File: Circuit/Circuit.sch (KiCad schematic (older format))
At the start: 47 parts, among them J1 Conn_01x20, J2 Conn_01x20, Q1 Q_NMOS_GDS, U1 STM32F103C8Tx, U2 AP131-33, U3 MCP2551-I-P, U4 MCP23017, U5 MC34063AP, Y1 8.000M, Y2 32.768K

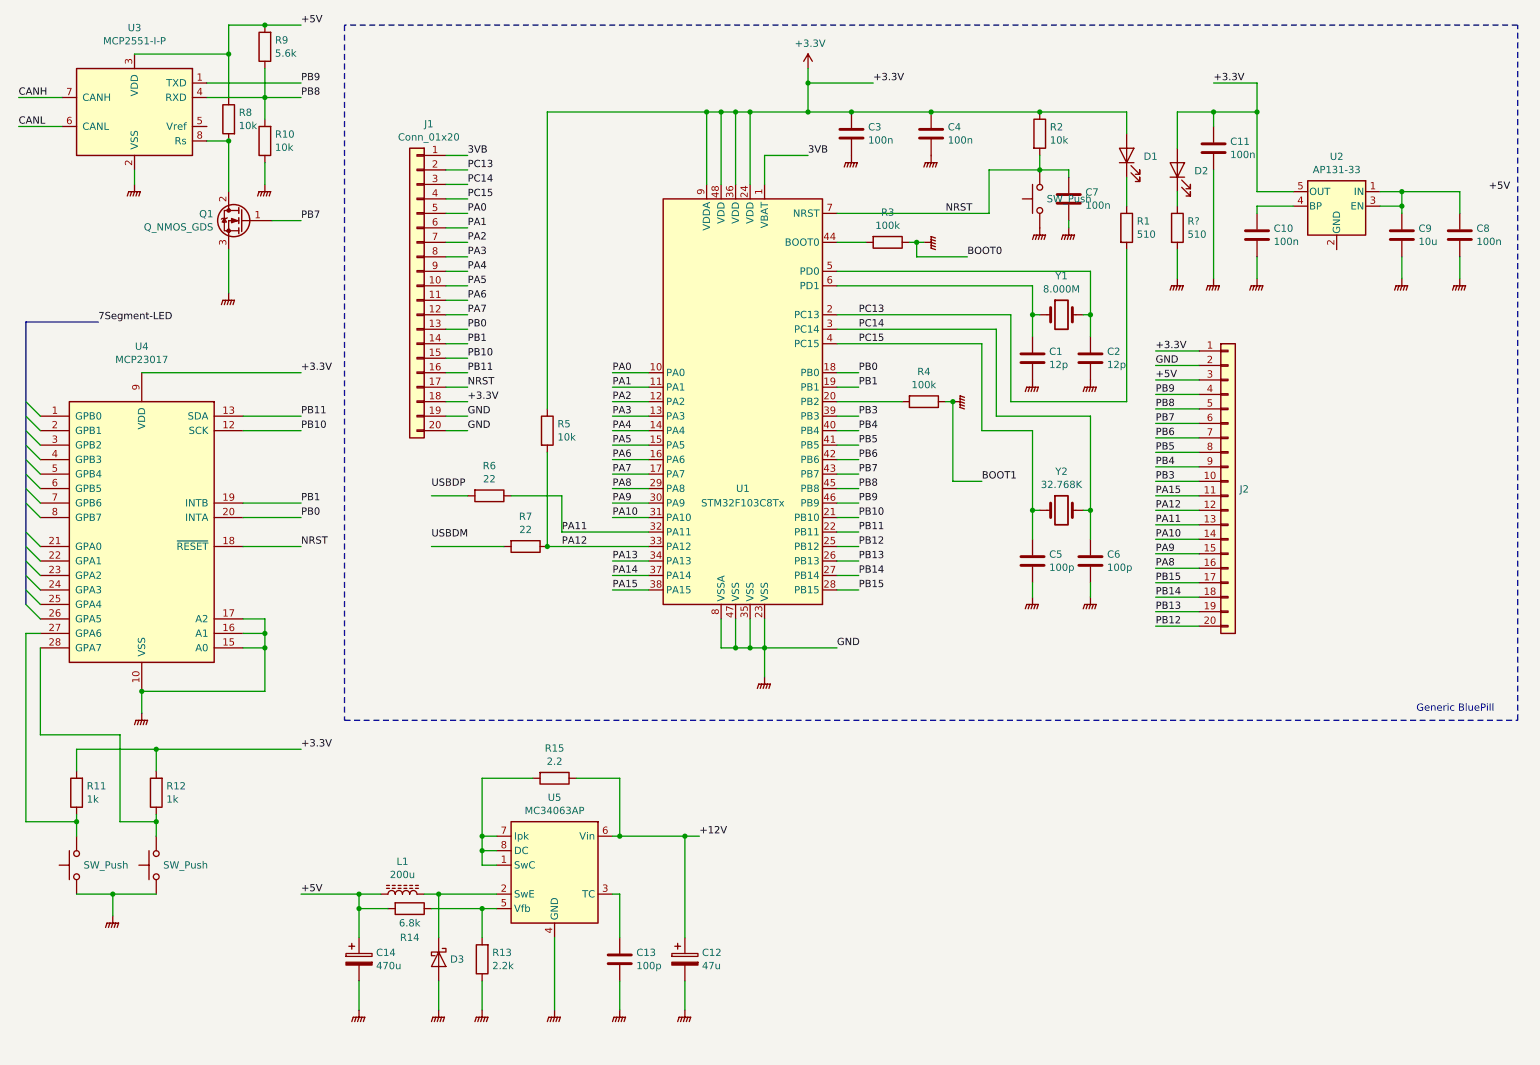
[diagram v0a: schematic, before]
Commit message: USB周りの自動生成ソースのライセンスがBSD 3-Clauseと同居できるのか怪しい感じなのでとりあえず除去
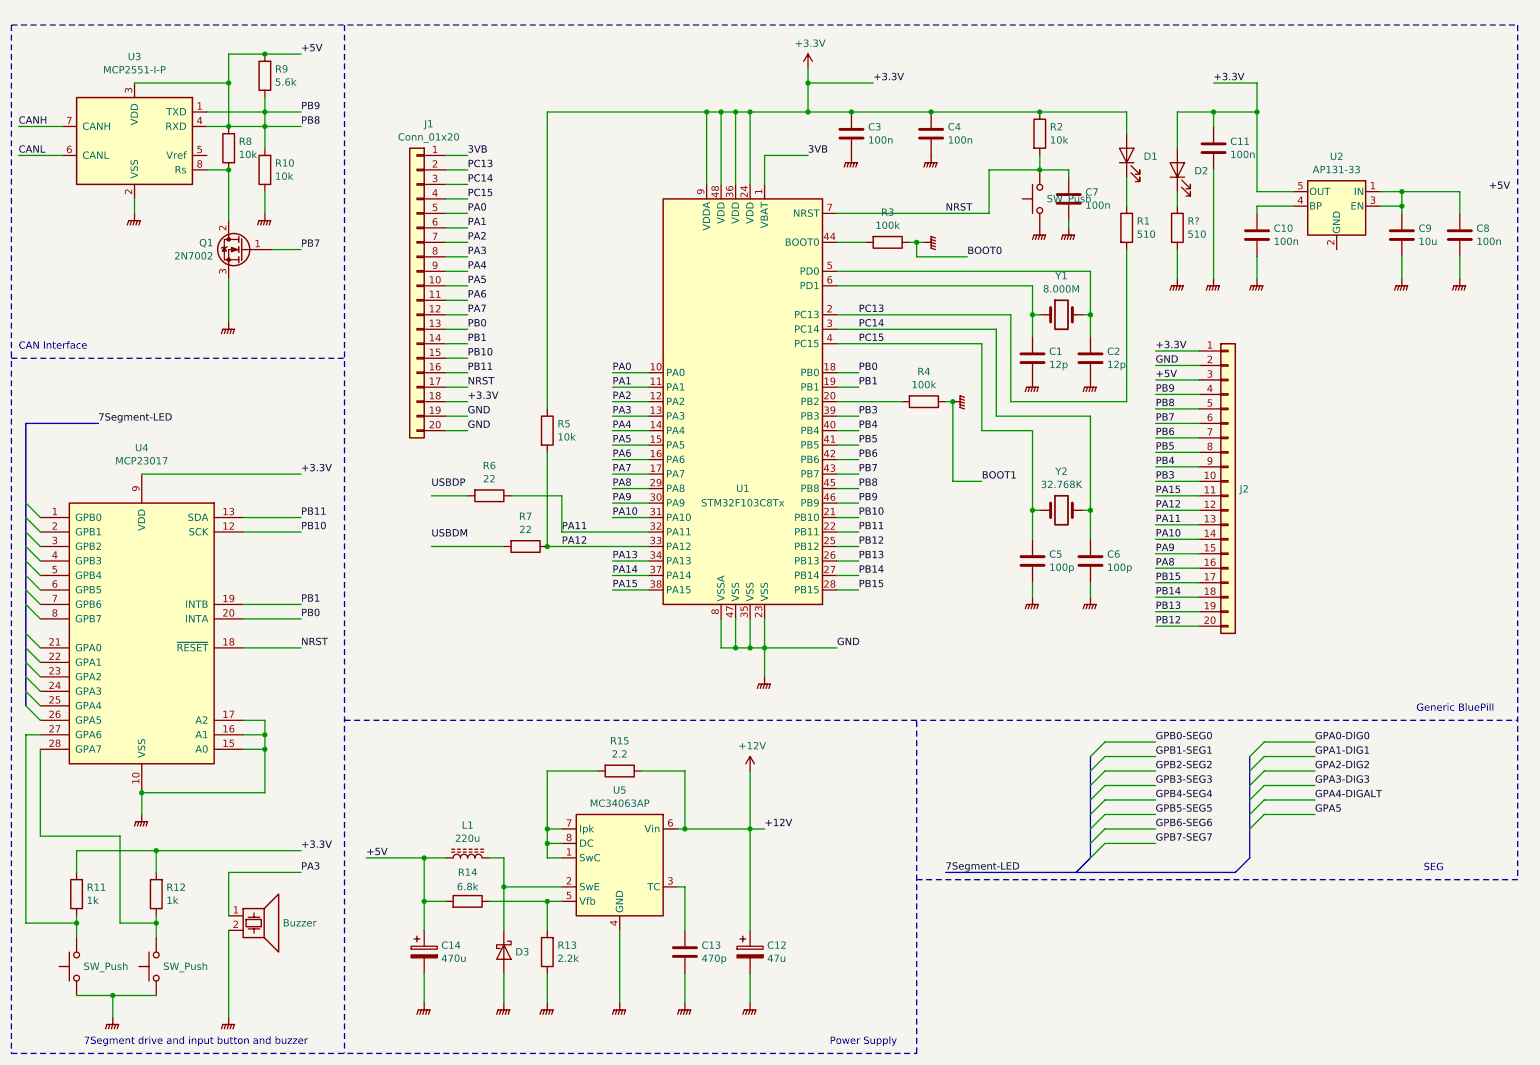
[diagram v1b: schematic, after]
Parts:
- added Buzzer: Speaker_Crystal, symbol Device:Speaker_Crystal
- C13: value 100p -> 470p
- L1: value 200u -> 220u
- Q1: value Q_NMOS_GDS -> 2N7002
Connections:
- net PB8 is gone; now on net +5V: J2.5 (Pin_5), R10.2, R9.1, U1.45 (PB8), U3.4 (RXD)
- net PB9 is gone; now on net +5V: J2.4 (Pin_4), U1.46 (PB9), U3.1 (TXD)
- net GNDPWR: now also Buzzer.2
- net PA3: now also Buzzer.1
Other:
- note added: "7Segment drive and input button and buzzer"
- note added: "CAN Interface"
- note added: "Power Supply"
- note added: "SEG"
- moved on the sheet: C12, C13, C14, D3, L1, Q1, R10, R11, R12, R13, R14, R15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
